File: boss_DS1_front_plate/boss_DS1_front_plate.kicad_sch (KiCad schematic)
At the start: 15 parts

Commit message: Updated front.
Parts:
- added D1: LED, pedale:red_led, symbol Device:LED
- added D2: LED, pedale:green_led, symbol Device:LED
- added J1: top_panel_connector, pedale:bottom_connector, symbol pedale:top_panel_connector
- added RV1, RV2, RV3: R_Potentiometer, pedale:top_plate_pot, symbol Device:R_Potentiometer
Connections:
- net 0: now also D1.1 (K), D2.1 (K)
- new net: J1.5 (Pin_5), RV2.1
- new net: J1.7 (Pin_7), RV2.2
- new net: J1.9 (Pin_9), RV2.3
- new net: J1.12 (Pin_12), RV3.1
- new net: J1.14 (Pin_14), RV3.2
- new net: J1.16 (Pin_16), RV3.3
- new net: D1.2 (A), J1.8 (Pin_8)
- new net: D2.2 (A), J1.10 (Pin_10)
- new net: J1.2 (Pin_2), RV1.1
- new net: J1.4 (Pin_4), RV1.2
- new net: J1.6 (Pin_6), RV1.3

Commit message: Potentiometers checked.
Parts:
- removed H10, H9: MountingHole, MountingHole:MountingHole_3mm, symbol Mechanical:MountingHole
- removed H5, H6, H7: MountingHole_Pad, pedale:plated_pot_hole, symbol Mechanical:MountingHole_Pad
- removed JP1, JP2, JP3, JP4: SolderJumper_2_Bridged, Jumper:SolderJumper-2_P1.3mm_Bridged_RoundedPad1.0x1.5mm, symbol Jumper:SolderJumper_2_Bridged
- removed RV1, RV2, RV3: R_Potentiometer, pedale:top_plate_pot, symbol Device:R_Potentiometer
- added RV1, RV2, RV3: pot_gnd, pedale:top_plate_pot, symbol pedale:pot_gnd
- J1: footprint pedale:bottom_connector -> Connector_IDC:IDC-Header_2x08_P2.54mm_Vertical
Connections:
- net 0: now also H8.1, J1.3 (GND), RV1.MH (2), RV2.MH (2), RV3.MH (2)
- net at J1.5 (Pin_5): now also RV2.1
- net at J1.7 (Pin_7): now also RV2.2
- net at J1.9 (Pin_9): now also RV2.3
- net at J1.12 (Pin_12): now also RV3.1
- net at J1.14 (Pin_14): now also RV3.2
- net at J1.16 (Pin_16): now also RV3.3
- net at J1.2 (Pin_2): now also RV1.1
- net at J1.4 (Pin_4): now also RV1.2
- net at J1.6 (Pin_6): now also RV1.3
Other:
- note added: "checked"
- moved on the sheet: D1, D2

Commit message: Pots again, done.
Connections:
- net at RV3.1: now also J1.16 (Pin_16); no longer J1.12 (Pin_12)
- net at RV3.3: now also J1.12 (Pin_12); no longer J1.16 (Pin_16)
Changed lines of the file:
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@@
 		(lib_id "pedale:top_panel_connector")
 		(at 45.72 77.47 0)
+		(mirror x)
 		(unit 3)
 		(exclude_from_sim no)
@@
 		(on_board yes)
 		(dnp no)
-		(fields_autoplaced yes)
 		(property "Reference" "J1"
-			(at 46.736 69.088 0)
+			(at 46.736 85.852 0)
 			(effects
 				(font
@@
 		)
 		(property "Value" "top_panel_connector"
-			(at 48.26 82.55 0)
+			(at 48.26 72.39 0)
 			(effects
 				(font
@@
 		)
 		(property "Description" ""
-			(at 31.75 117.094 0)
+			(at 31.75 37.846 0)
 			(effects
 				(font

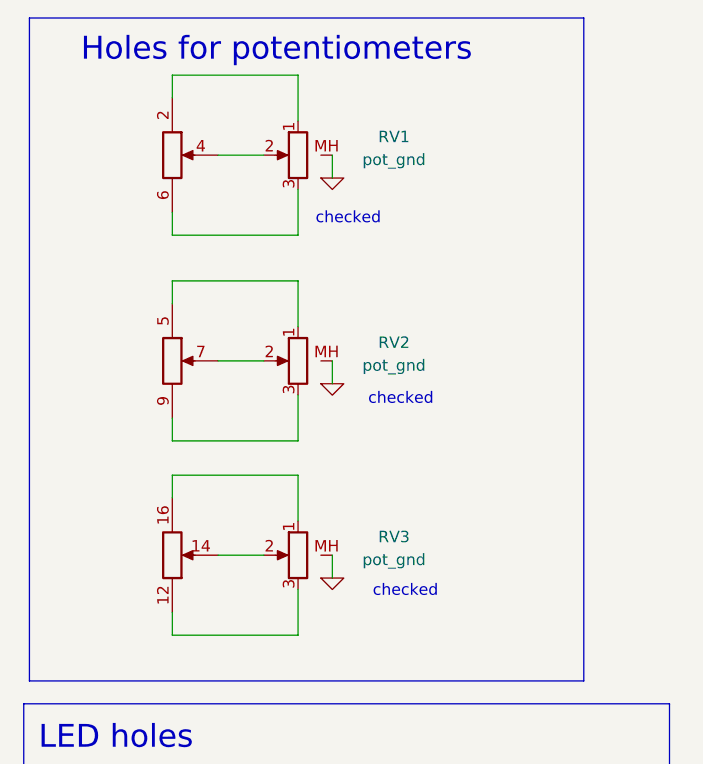
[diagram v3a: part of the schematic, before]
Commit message: Top plate routiran, valja proveriti pot-ove opet.
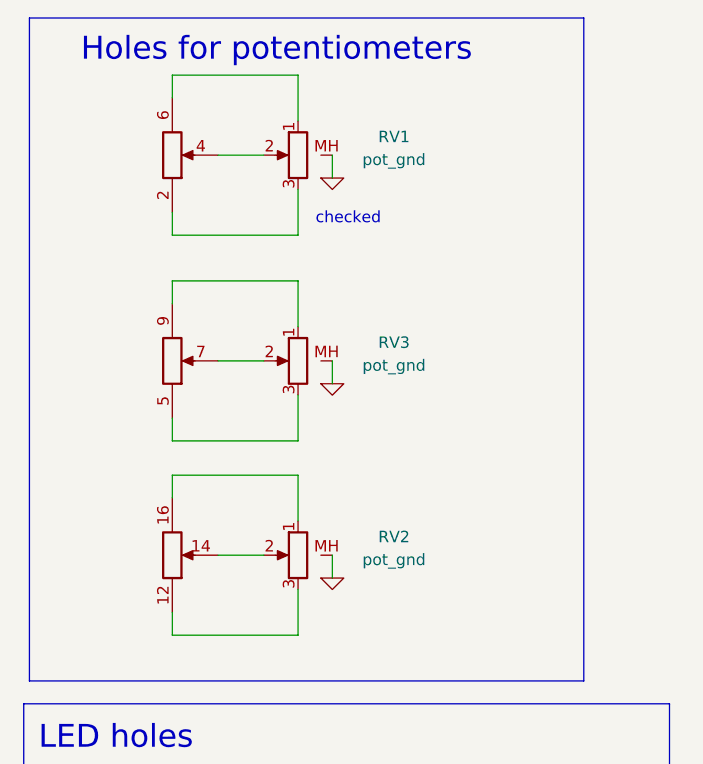
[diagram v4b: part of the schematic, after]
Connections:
- net at J1.5 (Pin_5): now also RV3.3; no longer RV2.1
- net at J1.7 (Pin_7): now also RV3.2; no longer RV2.2
- net at J1.9 (Pin_9): now also RV3.1; no longer RV2.3
- net at J1.2 (Pin_2): now also RV1.3; no longer RV1.1
- net at J1.6 (Pin_6): now also RV1.1; no longer RV1.3
- net at J1.16 (Pin_16): now also RV2.1; no longer RV3.1
- net at J1.14 (Pin_14): now also RV2.2; no longer RV3.2
- net at J1.12 (Pin_12): now also RV2.3; no longer RV3.3
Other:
- moved on the sheet: RV2, RV3

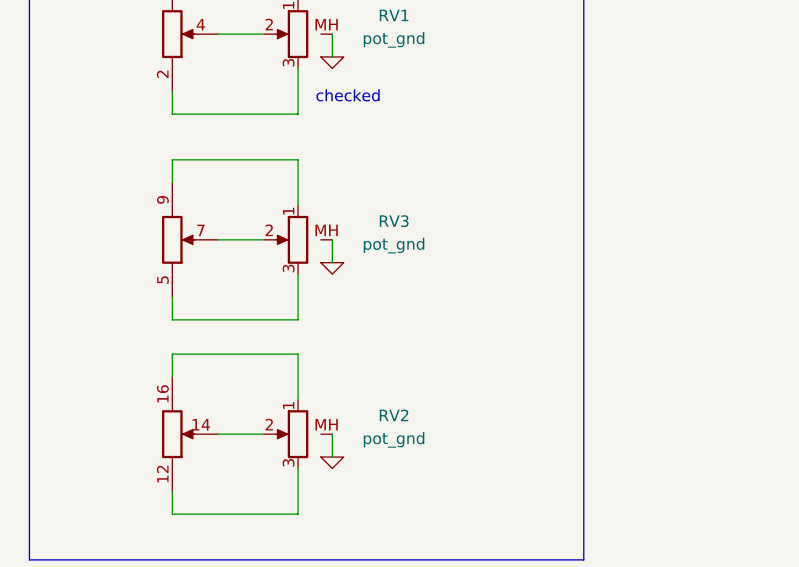
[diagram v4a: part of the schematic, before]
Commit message: Front plate update, diodes rotated.
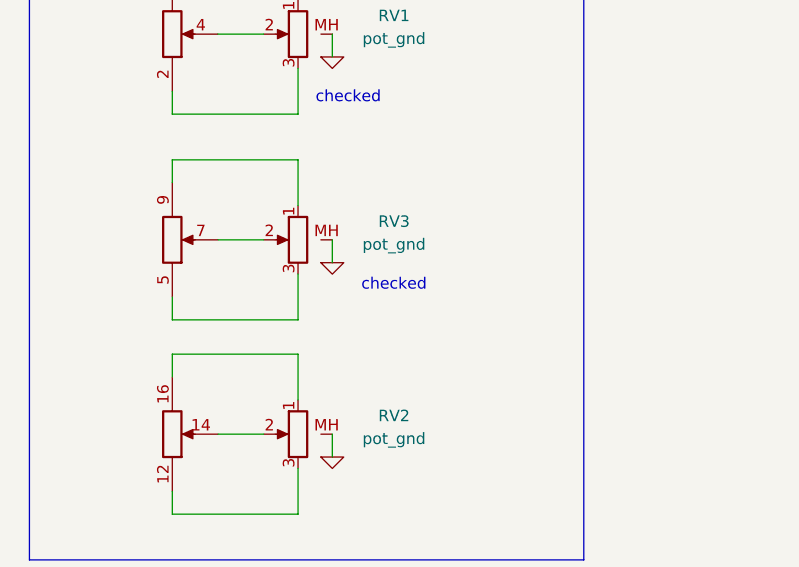
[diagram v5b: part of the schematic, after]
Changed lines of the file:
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@@
+		)
+	)
+	(text "checked\n"
+		(exclude_from_sim no)
+		(at 70.358 60.96 0)
+		(effects
+			(font
+				(size 1.27 1.27)
+			)
 		)
 	)
